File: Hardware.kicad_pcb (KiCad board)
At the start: 2 copper layers, 80 x 40 mm, 134 parts, among them J1 Conn_01x06_Socket, J2 JAE_SIM_Card_SF72S006, J3 Conn_Coaxial, J4 Conn_Coaxial, J5 Conn_01x05_Socket, J9 Battery, Q1 BC849, Q2 BC849, Q3 MMBT3904, Q4 BC849, Q5 MMBT3904, Q6 MMBT3904, SW1 SW_Push, SW3 SW_Push, U1 ESP32-WROOM-32, U10 MIC29302AWD, U11 AMS1117-3.3, U13 MC34063AD, U2 NEO-M8M, U3 SN65HVD231, U4 BQ24075RGT, U5 AT24CS01-XHM, U6 A7670E, U7 AMS1117-3.3, U9 AMS1117-3.3

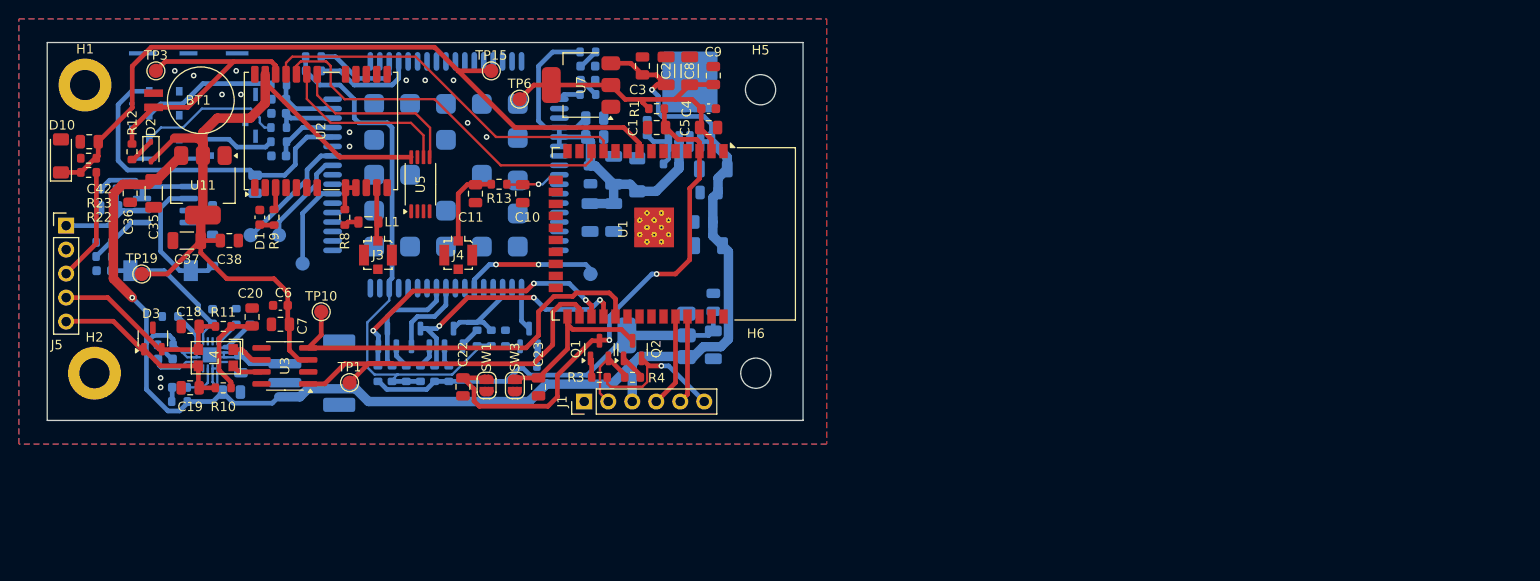
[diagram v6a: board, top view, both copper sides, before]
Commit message: updated schematics:
Fixed bug with PWKEY of LTE module

Fixed big with power
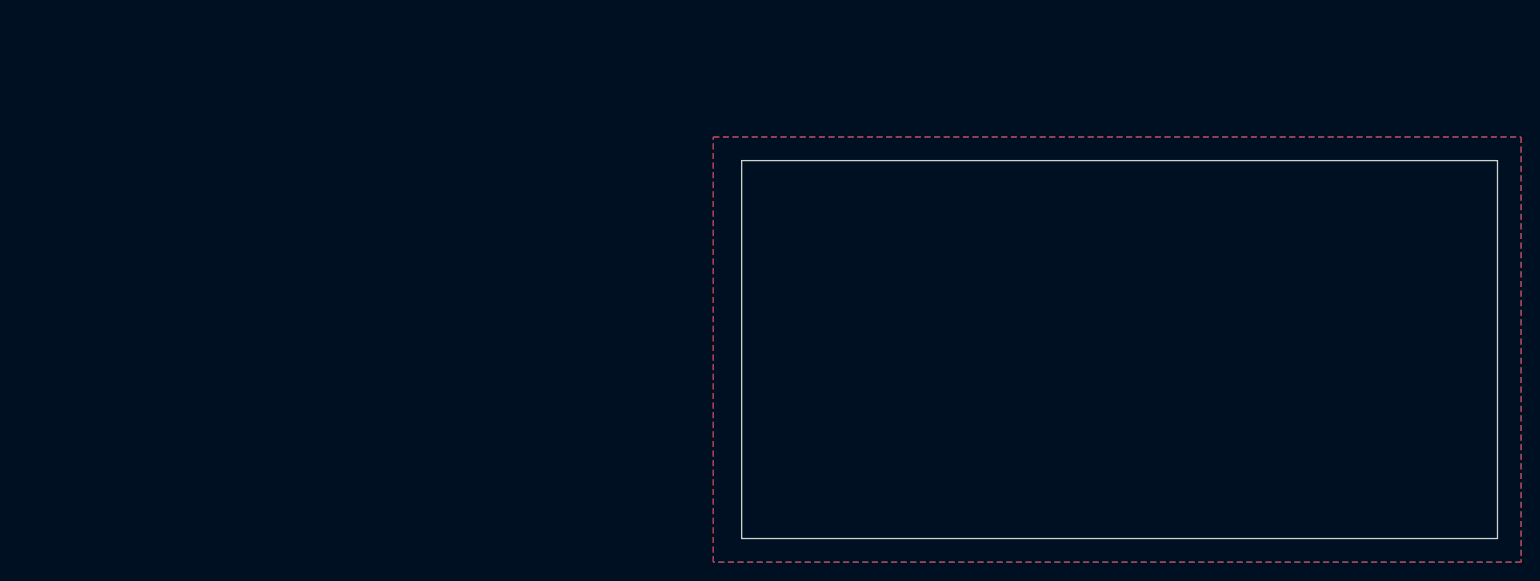
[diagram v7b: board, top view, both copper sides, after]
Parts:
- removed BT1: Battery_Cell, Battery:BatteryHolder_Seiko_MS621F
- removed C1, C22, C23, C46, C5, C7: 0.1uF, Capacitor_SMD:C_0805_2012Metric
- removed C10, C11: NC, Capacitor_SMD:C_0805_2012Metric
- removed C14, C2, C21, C25, C31, C33, C35, C37, C49, C8: 10uF, Capacitor_SMD:C_1206_3216Metric
- removed C17, C18, C19, C24, C26, C3, C32, C34, C36, C38, C42, C44, C50, C9: 100pF, Capacitor_SMD:C_0805_2012Metric
- removed C20, C39, C40: 4.7uF, Capacitor_SMD:C_0805_2012Metric
- removed C4, C41, C43, C45, C6: 22uF, Capacitor_SMD:C_0603_1608Metric
- removed C47, C48: 470pF, Capacitor_SMD:C_0603_1608Metric
- removed C51: 1uF, Capacitor_SMD:C_0603_1608Metric
- removed D1, D4, D5, D7, D8: LED, Capacitor_SMD:C_0603_1608Metric
- removed D10, D6: BZV55B5V1, Diode_SMD:D_MiniMELF
- removed D12: 1N5819, Diode_SMD:D_SOD-123
- removed D2: 1N4148, Diode_SMD:D_SOD-323
- removed D3: PESD1CAN, Package_TO_SOT_SMD:SOT-23-3
- removed H1, H2: MountingHole_Pad, MountingHole:MountingHole_3.2mm_M3_DIN965_Pad
- removed H5, H6: MountingHole, MountingHole:MountingHole_3.2mm_M3
- removed J1: Conn_01x06_Socket, Connector_PinHeader_2.54mm:PinHeader_1x06_P2.54mm_Vertical
- removed J2: JAE_SIM_Card_SF72S006, Connector_JAE:JAE_SIM_Card_SF72S006
- removed J3, J4: Conn_Coaxial, Connector_Coaxial:U.FL_Molex_MCRF_73412-0110_Vertical
- removed J5: Conn_01x05_Socket, Connector_PinHeader_2.54mm:PinHeader_1x05_P2.54mm_Vertical
- removed J9: Battery, Connector_JST:JST_PH_S2B-PH-SM4-TB_1x02-1MP_P2.00mm_Horizontal
- removed L1: 27uH, Inductor_SMD:L_0805_2012Metric
- removed L4: EPCO B82787C0513, EPCO_B82787C0513:EPCO B82787C0513
- removed L6: 220uH, Inductor_SMD:L_7.3x7.3_H4.5
- removed Q1, Q2, Q4: BC849, Package_TO_SOT_SMD:SOT-23
- removed Q3, Q5, Q6: MMBT3904, Package_TO_SOT_SMD:SOT-23
- removed R1, R22, R3, R4, R52, R6: 10K, Resistor_SMD:R_0603_1608Metric
- removed R10, R11: 60R, Resistor_SMD:R_0603_1608Metric
- removed R12: 120R, Resistor_SMD:R_0603_1608Metric
- removed R13: R33, Resistor_SMD:R_0603_1608Metric
- removed R17, R43: 51R, Resistor_SMD:R_0603_1608Metric
- removed R18, R48: 100K, Resistor_SMD:R_0603_1608Metric
- removed R19, R20, R41, R46, R47, R49, R50: 4K7, Resistor_SMD:R_0603_1608Metric
- removed R2, R44, R45, R5, R9: 1K, Resistor_SMD:R_0603_1608Metric
- removed R21: 1k18, Resistor_SMD:R_0603_1608Metric
- removed R23: 3K9, Resistor_SMD:R_0603_1608Metric
- removed R24, R25, R26, R8: 22R, Resistor_SMD:R_0603_1608Metric
- removed R29: 0.33R, Resistor_SMD:R_0603_1608Metric
- removed R30: 3K3, Resistor_SMD:R_0603_1608Metric
- removed R31: 1K2, Resistor_SMD:R_0603_1608Metric
- removed R42: 47K, Resistor_SMD:R_0603_1608Metric
- removed R51: 22K, Resistor_SMD:R_0603_1608Metric
- removed R7: 1k13, Resistor_SMD:R_0603_1608Metric
- removed SW1, SW3: SW_Push, Jumper:SolderJumper-2_P1.3mm_Open_RoundedPad1.0x1.5mm
- removed TP1, TP10, TP11, TP15, TP19, TP3, TP6, TP7, TP8, TP9: TestPoint, TestPoint:TestPoint_Pad_D1.5mm
- removed U1: ESP32-WROOM-32, RF_Module:ESP32-WROOM-32
- removed U10: MIC29302AWD, Package_TO_SOT_SMD:TO-252-5_TabPin3
- removed U11, U7, U9: AMS1117-3.3, Package_TO_SOT_SMD:SOT-223-3_TabPin2
- removed U13: MC34063AD, Package_SO:SOIC-8_3.9x4.9mm_P1.27mm
- removed U2: NEO-M8M, RF_GPS:ublox_NEO
- removed U3: SN65HVD231, Package_SO:SOIC-8_3.9x4.9mm_P1.27mm
- removed U4: BQ24075RGT, Package_DFN_QFN:VQFN-16-1EP_3x3mm_P0.5mm_EP1.6x1.6mm
- removed U5: AT24CS01-XHM, Package_SO:TSSOP-8_4.4x3mm_P0.65mm
- removed U6: A7670E, A7670E:A7670E
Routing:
- net +5V: track 159.8 -> 0.00 mm, vias 2 -> 0
- net PSU_GPS: track 80.5 -> 0.00 mm
- net /ACC_Readout: track 78.6 -> 0.00 mm
- net /LTE_Module/1V8: track 59.5 -> 0.00 mm
- net /EN: track 56.5 -> 0.00 mm, vias 2 -> 0
- net /LTE_Module/VBAT: track 45.5 -> 0.00 mm
- net CAN_RX: track 42.9 -> 0.00 mm
- net /LTE_Module/3V3: track 41.2 -> 0.00 mm
- net CAN_TX: track 40.6 -> 0.00 mm
- net GPS_RX: track 39.9 -> 0.00 mm
- net GPS_TX: track 39.2 -> 0.00 mm
- net /LTE_Module/SIM_VCC: track 35.8 -> 0.00 mm
- net /PSU: track 31.6 -> 0.00 mm
- net LTE_RX: track 31.2 -> 0.00 mm, vias 3 -> 0
- net Gps_V_Back: track 29.5 -> 0.00 mm
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
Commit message: first new layout
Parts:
- added BT1: Battery_Cell, Battery:BatteryHolder_Seiko_MS621F, B.Cu at (146.3, 65.1)
- added C1: 100nF, Capacitor_SMD:C_0805_2012Metric, F.Cu at (176.8, 71.5)
- added C10: NC, Capacitor_SMD:C_0805_2012Metric, B.Cu at (131.0, 88.6)
- added C11: NC, Capacitor_SMD:C_0805_2012Metric, B.Cu at (129.5, 85.5)
- added C12: 100nF, Capacitor_SMD:C_0805_2012Metric, B.Cu at (145.4, 88.5)
- added C13: 22uF, Capacitor_SMD:C_0603_1608Metric, B.Cu at (150.5, 98.5)
- added C14: 10uF, Capacitor_SMD:C_1206_3216Metric, F.Cu at (131.5, 99.0)
- added C15: 150pF, Capacitor_SMD:C_0603_1608Metric, B.Cu at (142.9, 95.4)
- added C16: NC, Capacitor_SMD:C_0805_2012Metric, B.Cu at (145.5, 96.0)
- added C17: 100pF, Capacitor_SMD:C_0805_2012Metric, F.Cu at (128.0, 95.5)
- added C18: 100pF, Capacitor_SMD:C_0805_2012Metric, B.Cu at (123.0, 99.6)
- added C19: 100pF, Capacitor_SMD:C_0805_2012Metric, B.Cu at (123.0, 91.7)
- added C2: 10uF, Capacitor_SMD:C_1206_3216Metric, F.Cu at (163.5, 69.5)
- added C20: 4.7uF, Capacitor_SMD:C_0805_2012Metric, B.Cu at (127.0, 99.6)
- added C21: 10uF, Capacitor_SMD:C_1206_3216Metric, F.Cu at (128.0, 100.0)
- added C22: 100nF, Capacitor_SMD:C_0805_2012Metric, F.Cu at (163.4, 97.0)
- added C23: 100nF, Capacitor_SMD:C_0805_2012Metric, F.Cu at (163.4, 95.0)
- added C24: 100pF, Capacitor_SMD:C_0805_2012Metric, F.Cu at (131.9, 95.5)
- added C27: 10uF, Capacitor_SMD:C_1206_3216Metric, B.Cu at (140.5, 84.5)
- added C3: 100pF, Capacitor_SMD:C_0805_2012Metric, F.Cu at (163.5, 65.0)
- added C30: 4.7uF, Capacitor_SMD:C_0805_2012Metric, B.Cu at (163.8, 90.0)
- added C33: 10uF, Capacitor_SMD:C_1206_3216Metric, F.Cu at (153.5, 98.0)
- added C34: 100pF, Capacitor_SMD:C_0805_2012Metric, F.Cu at (156.0, 97.5)
- added C35: 10uF, Capacitor_SMD:C_1206_3216Metric, B.Cu at (156.9, 76.5)
- added C36: 100pF, Capacitor_SMD:C_0805_2012Metric, B.Cu at (152.4, 76.5)
- added C37: 10uF, Capacitor_SMD:C_1206_3216Metric, B.Cu at (156.9, 66.5)
- added C38: 100pF, Capacitor_SMD:C_0805_2012Metric, B.Cu at (152.4, 66.5)
- added C39: 4.7uF, Capacitor_SMD:C_0805_2012Metric, B.Cu at (163.8, 93.5)
- added C4: 22uF, Capacitor_SMD:C_0603_1608Metric, F.Cu at (180.5, 72.0)
- added C42: 100pF, Capacitor_SMD:C_0805_2012Metric, F.Cu at (116.3, 84.0)
- added C44: 100pF, Capacitor_SMD:C_0805_2012Metric, F.Cu at (160.5, 66.5)
- added C46: 1uF, Capacitor_SMD:C_0603_1608Metric, B.Cu at (159.5, 86.6)
- added C49: 10uF, Capacitor_SMD:C_1206_3216Metric, F.Cu at (134.0, 99.0)
- added C5: 100nF, Capacitor_SMD:C_0805_2012Metric, F.Cu at (180.0, 69.0)
- added C50: 100pF, Capacitor_SMD:C_0805_2012Metric, F.Cu at (128.0, 97.5)
- added C6: 22uF, Capacitor_SMD:C_0603_1608Metric, B.Cu at (133.9, 99.1)
- added C7: 100nF, Capacitor_SMD:C_0805_2012Metric, B.Cu at (130.4, 99.0)
- added C8: 10uF, Capacitor_SMD:C_1206_3216Metric, F.Cu at (173.5, 69.5)
- added C9: 100pF, Capacitor_SMD:C_0805_2012Metric, F.Cu at (173.5, 65.0)
- added D1: LED, Capacitor_SMD:C_0603_1608Metric, B.Cu at (143.0, 79.0)
- added D10: BZV55B5V1, Diode_SMD:D_MiniMELF, F.Cu at (116.4, 91.5)
- added D2: 1N4148, Diode_SMD:D_SOD-323, B.Cu at (149.0, 75.5)
- added D3: PESD1CAN, Package_TO_SOT_SMD:SOT-23-3, B.Cu at (120.0, 95.5)
- added D4: LED, Capacitor_SMD:C_0603_1608Metric, F.Cu at (122.7, 97.0)
- added D5: LED, Capacitor_SMD:C_0603_1608Metric, F.Cu at (122.7, 100.5)
- added D6: BZV55B5V1, Diode_SMD:D_MiniMELF, F.Cu at (143.5, 97.0)
- added D7: LED, Capacitor_SMD:C_0603_1608Metric, B.Cu at (161.0, 94.7)
- added D8: LED, Capacitor_SMD:C_0603_1608Metric, B.Cu at (157.5, 94.7)
- added D9: BZV55B5V1, Diode_SMD:D_MiniMELF, B.Cu at (150.5, 86.0)
- added H1: MountingHole_Pad, MountingHole:MountingHole_3.2mm_M3_DIN965_Pad, F.Cu at (114.0, 66.5)
- added H2: MountingHole_Pad, MountingHole:MountingHole_3.2mm_M3_DIN965_Pad, F.Cu at (114.0, 97.5)
- added H5: MountingHole, MountingHole:MountingHole_3.2mm_M3, F.Cu at (184.5, 67.5)
- added H6: MountingHole, MountingHole:MountingHole_3.2mm_M3, F.Cu at (184.5, 97.5)
- added J1: Conn_01x06_Socket, Connector_PinHeader_2.54mm:PinHeader_1x06_P2.54mm_Vertical, F.Cu at (166.4, 100.0)
- added J2: JAE_SIM_Card_SF72S006, Connector_JAE:JAE_SIM_Card_SF72S006, F.Cu at (153.9, 67.8)
- added J3: Conn_Coaxial, Connector_Coaxial:U.FL_Molex_MCRF_73412-0110_Vertical, B.Cu at (124.5, 80.9)
- added J4: Conn_Coaxial, Connector_Coaxial:U.FL_Molex_MCRF_73412-0110_Vertical, B.Cu at (124.5, 87.0)
- added J5: Conn_01x05_Socket, Connector_PinHeader_2.54mm:PinHeader_1x05_P2.54mm_Vertical, F.Cu at (112.0, 81.4)
- added J9: Battery, Connector_JST:JST_PH_S2B-PH-SM4-TB_1x02-1MP_P2.00mm_Horizontal, B.Cu at (164.5, 78.0)
- added L1: 27uH, Inductor_SMD:L_0805_2012Metric, B.Cu at (129.3, 79.4)
- added L2: 15uH, Inductor_SMD:L_Abracon_ASPI-0630LR, B.Cu at (150.5, 92.5)
- added L4: EPCO B82787C0513, EPCO_B82787C0513:EPCO B82787C0513, B.Cu at (125.0, 95.6)
- added Q1: BC849, Package_TO_SOT_SMD:SOT-23, F.Cu at (172.5, 94.7)
- added Q2: BC849, Package_TO_SOT_SMD:SOT-23, F.Cu at (169.0, 94.7)
- added Q3: MMBT3904, Package_TO_SOT_SMD:SOT-23, F.Cu at (157.9, 87.6)
- added Q4: BC849, Package_TO_SOT_SMD:SOT-23, F.Cu at (154.4, 87.6)
- added Q5: MMBT3904, Package_TO_SOT_SMD:SOT-23, F.Cu at (151.6, 80.0)
- added Q6: MMBT3904, Package_TO_SOT_SMD:SOT-23, F.Cu at (151.6, 83.5)
- added R1: 10K, Resistor_SMD:R_0603_1608Metric, F.Cu at (176.8, 69.5)
- added R10: 60R, Resistor_SMD:R_0603_1608Metric, B.Cu at (125.0, 91.6)
- added R11: 60R, Resistor_SMD:R_0603_1608Metric, B.Cu at (125.0, 99.6)
- added R12: 120R, Resistor_SMD:R_0603_1608Metric, B.Cu at (147.0, 75.5)
- added R13: R33, Resistor_SMD:R_0603_1608Metric, B.Cu at (128.5, 88.0)
- added R14: 10K, Resistor_SMD:R_0603_1608Metric, B.Cu at (163.5, 86.6)
- added R15: 40K2, Resistor_SMD:R_0603_1608Metric, B.Cu at (139.9, 95.4)
- added R16: 210K, Resistor_SMD:R_0603_1608Metric, B.Cu at (139.9, 96.9)
- added R17: 51R, Resistor_SMD:R_0603_1608Metric, F.Cu at (122.7, 95.5)
- added R18: 100K, Resistor_SMD:R_0603_1608Metric, F.Cu at (159.5, 91.1)
- added R19: 4K7, Resistor_SMD:R_0603_1608Metric, F.Cu at (156.5, 91.1)
- added R2: 1K, Resistor_SMD:R_0603_1608Metric, B.Cu at (159.5, 94.7)
- added R20: 4K7, Resistor_SMD:R_0603_1608Metric, F.Cu at (158.0, 91.1)
- added R21: 100K, Resistor_SMD:R_0603_1608Metric, B.Cu at (142.9, 96.9)
- added R22: 10K, Resistor_SMD:R_0603_1608Metric, F.Cu at (116.3, 86.0)
- added R23: 3K9, Resistor_SMD:R_0603_1608Metric, F.Cu at (116.3, 87.5)
- added R24: 22R, Resistor_SMD:R_0603_1608Metric, F.Cu at (142.5, 66.0)
- added R25: 22R, Resistor_SMD:R_0603_1608Metric, F.Cu at (142.5, 64.5)
- added R26: 22R, Resistor_SMD:R_0603_1608Metric, F.Cu at (142.5, 63.0)
- added R27: 100K, Resistor_SMD:R_0603_1608Metric, B.Cu at (140.0, 82.5)
- added R3: 10K, Resistor_SMD:R_0603_1608Metric, F.Cu at (174.9, 95.2)
- added R4: 10K, Resistor_SMD:R_0603_1608Metric, F.Cu at (166.4, 95.2)
- added R41: 4K7, Resistor_SMD:R_0603_1608Metric, F.Cu at (155.0, 91.1)
- added R42: 47K, Resistor_SMD:R_0603_1608Metric, F.Cu at (153.5, 91.1)
- added R43: 51R, Resistor_SMD:R_0603_1608Metric, F.Cu at (122.7, 99.0)
- added R44: 1K, Resistor_SMD:R_0603_1608Metric, F.Cu at (115.8, 73.8)
- added R45: 1K, Resistor_SMD:R_0603_1608Metric, F.Cu at (117.3, 73.8)
- added R46: 4K7, Resistor_SMD:R_0603_1608Metric, F.Cu at (155.2, 81.5)
- added R47: 4K7, Resistor_SMD:R_0603_1608Metric, F.Cu at (155.2, 80.0)
- added R48: 100K, Resistor_SMD:R_0603_1608Metric, F.Cu at (155.2, 78.5)
- added R49: 4K7, Resistor_SMD:R_0603_1608Metric, F.Cu at (155.2, 84.5)
- added R5: 1K, Resistor_SMD:R_0603_1608Metric, B.Cu at (156.0, 94.7)
- added R50: 4K7, Resistor_SMD:R_0603_1608Metric, F.Cu at (155.2, 83.0)
- added R51: 22K, Resistor_SMD:R_0603_1608Metric, F.Cu at (149.5, 88.5)
- added R52: 10K, Resistor_SMD:R_0603_1608Metric, F.Cu at (147.0, 88.5)
- added R6: 1k18, Resistor_SMD:R_0603_1608Metric, B.Cu at (158.0, 86.6)
- added R7: 1k13, Resistor_SMD:R_0603_1608Metric, B.Cu at (162.0, 86.6)
- added R8: 22R, Resistor_SMD:R_0603_1608Metric, B.Cu at (132.8, 79.4)
- added R9: 1K, Resistor_SMD:R_0603_1608Metric, B.Cu at (140.0, 79.0)
- added SW1: SW_Push, Jumper:SolderJumper-2_P1.3mm_Open_RoundedPad1.0x1.5mm, F.Cu at (163.0, 99.7)
- added SW3: SW_Push, Jumper:SolderJumper-2_P1.3mm_Open_RoundedPad1.0x1.5mm, F.Cu at (160.5, 99.7)
- added TP11: TestPoint, TestPoint:TestPoint_Pad_D1.5mm, F.Cu at (118.0, 63.5)
- added TP2: TestPoint, TestPoint:TestPoint_Pad_D1.5mm, B.Cu at (155.0, 87.0)
- added TP7: TestPoint, TestPoint:TestPoint_Pad_D1.5mm, F.Cu at (147.0, 82.5)
- added TP8: TestPoint, TestPoint:TestPoint_Pad_D1.5mm, F.Cu at (121.0, 66.5)
- added TP9: TestPoint, TestPoint:TestPoint_Pad_D1.5mm, F.Cu at (121.0, 63.5)
- added U1: ESP32-WROOM-32, RF_Module:ESP32-WROOM-32, F.Cu at (172.8, 82.8)
- added U10: MIC29302AWD, Package_TO_SOT_SMD:TO-252-5_TabPin3, F.Cu at (148.8, 97.0)
- added U11: AMS1117-3.3, Package_TO_SOT_SMD:SOT-223-3_TabPin2, B.Cu at (154.8, 71.5)
- added U2: NEO-M8M, RF_GPS:ublox_NEO, B.Cu at (134.3, 71.0)
- added U3: SN65HVD231, Package_SO:SOIC-8_3.9x4.9mm_P1.27mm, B.Cu at (132.5, 95.1)
- added U4: BQ24075RGT, Package_DFN_QFN:VQFN-16-1EP_3x3mm_P0.5mm_EP1.6x1.6mm, B.Cu at (160.4, 90.4)
- added U5: AT24CS01-XHM, Package_SO:TSSOP-8_4.4x3mm_P0.65mm, B.Cu at (124.0, 71.0)
- added U6: A7670E, A7670E:A7670E, F.Cu at (132.0, 80.8)
- added U7: AMS1117-3.3, Package_TO_SOT_SMD:SOT-223-3_TabPin2, F.Cu at (168.5, 67.5)
- added U8: MP1584EN, SOIC127P600X170-9N:SOIC127P600X170-9N, B.Cu at (141.4, 90.4)
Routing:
- net +3V3: track 0.00 -> 175.5 mm, vias 0 -> 5
- net +5V: track 0.00 -> 121.6 mm, vias 0 -> 4
- net /ACC_Readout: track 0.00 -> 91.5 mm, vias 0 -> 2
- net /LTE_Module/1V8: track 0.00 -> 72.1 mm
- net /LTE_Module/SIM_VCC: track 0.00 -> 52.4 mm
- net GPS_TX: track 0.00 -> 50.9 mm, vias 0 -> 1
- net /LTE_Module/VBAT: track 0.00 -> 47.3 mm
- net CAN_TX: track 0.00 -> 44.6 mm, vias 0 -> 1
- net CAN_RX: track 0.00 -> 44.0 mm, vias 0 -> 1
- net GPS_RX: track 0.00 -> 43.4 mm, vias 0 -> 1
- net /EN: track 0.00 -> 42.1 mm, vias 0 -> 3
- net PW+: track 0.00 -> 39.2 mm
- net LTE_TX: track 0.00 -> 32.0 mm, vias 0 -> 2
- net LTE_RX: track 0.00 -> 29.4 mm, vias 0 -> 2
- net +BATT: track 0.00 -> 24.1 mm
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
